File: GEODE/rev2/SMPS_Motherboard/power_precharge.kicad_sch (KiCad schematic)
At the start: 20 parts, among them IC1501 TPS2490DGSRG4, Q1101 SOT233 ZXMP10A13F, Q1102 SOT233 BSS123N

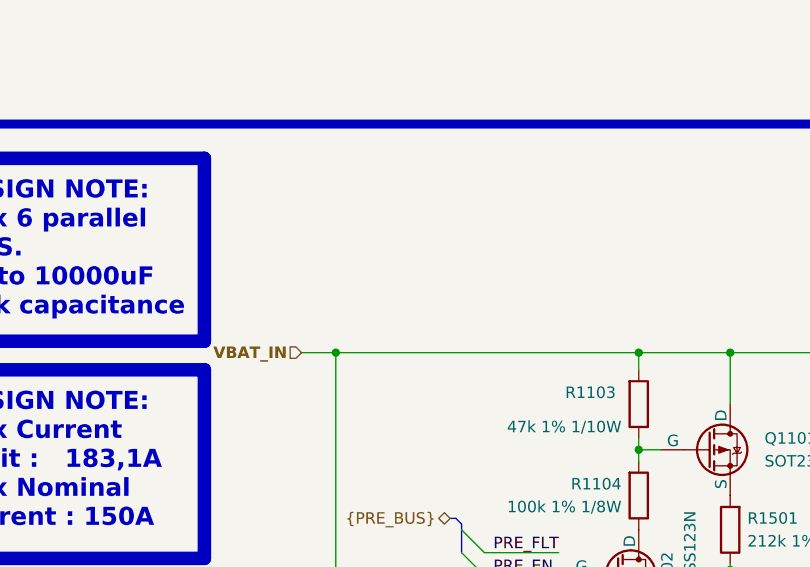
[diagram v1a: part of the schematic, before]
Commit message: changed connectors, removed can, added fuse, disconnected EXTVCC in power generation
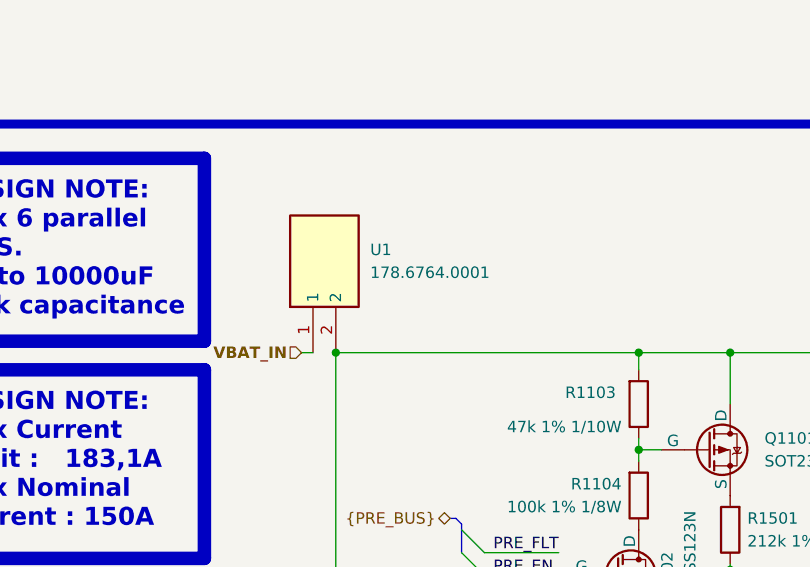
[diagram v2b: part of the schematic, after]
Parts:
- added U1: 178.6764.0001, 17867640001, symbol SamacSys_Parts:178.6764.0001
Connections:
- net VBAT_IN: now also U1.1; no longer C1501.1, NT1101.2, Q1101.3 (D), R1103.2, R1505.1
- new net Vsense_high: C1501.1, NT1101.2, Q1101.3 (D), R1103.2, R1505.1, U1.2
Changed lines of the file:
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@@
+	)
+	(junction
+		(at 87.63 68.58)
+		(diameter 0)
+		(color 0 0 0 0)
 	)
 	(junction
@@
 	)
 	(junction
-		(at 87.63 68.58)
-		(diameter 0)
-		(color 0 0 0 0)
-	)
-	(junction
 		(at 156.21 114.935)
 		(diameter 0)
@@
 	(wire
 		(pts
-			(xy 83.82 68.58) (xy 87.63 68.58)
-		)
-		(stroke
-			(width 0)
-			(type default)
-		)
-	)
-	(wire
-		(pts
 			(xy 87.63 115.57) (xy 87.63 114.935)
 		)
@@
 		(pts
 			(xy 188.595 95.25) (xy 198.755 95.25)
+		)
+		(stroke
+			(width 0)
+			(type default)
+		)
+	)
+	(wire
+		(pts
+			(xy 83.82 68.58) (xy 85.09 68.58)
 		)
 		(stroke
@@
 					(unit 1)
 				)
+			)
+		)
+	)
+	(symbol
+		(lib_id "SamacSys_Parts:178.6764.0001")
+		(at 85.09 68.58 90)
+		(unit 1)
+		(exclude_from_sim no)
+		(in_bom yes)
+		(on_board yes)
+		(dnp no)
+		(fields_autoplaced yes)
+		(property "Reference" "U1"
+			(at 91.44 57.1499 90)
+			(effects
+				(font
+					(size 1.27 1.27)
+				)
+				(justify right)
+			)
+		)
+		(property "Value" "178.6764.0001"
+			(at 91.44 59.6899 90)
+			(effects
+				(font
+					(size 1.27 1.27)
+				)
+				(justify right)
+			)
+		)
+		(property "Footprint" "17867640001"
+			(at 180.01 52.07 0)
+			(effects
+				(font
+					(size 1.27 1.27)
+				)
+				(justify left top)
+				(hide yes)
+			)
+		)
+		(property "Datasheet" "http://www.littelfuse.com/~/media/commercial-vehicle/datasheets/automotive-fuse-holders/mini/littelfuse-fuseholder-mini-fl1-pcb-mount.pdf"
+			(at 280.01 52.07 0)
+			(effects
+				(font
+					(size 1.27 1.27)
+				)
+				(justify left top)
+				(hide yes)
+			)
+		)
+		(property "Description" "LITTELFUSE - 178.6764.0001 - FUSE HOLDER, PCB, FK1 BLADE"
+			(at 85.09 68.58 0)
+			(effects
+				(font
+					(size 1.27 1.27)
+				)
+				(hide yes)
+			)
+		)
+		(property "Height" "15"
+			(at 480.01 52.07 0)
+			(effects
+				(font
+					(size 1.27 1.27)
+				)
+				(justify left top)
+				(hide yes)
+			)
+		)
+		(property "Mouser Part Number" "576-178.6764.0001"
+			(at 580.01 52.07 0)
+			(effects
+				(font
+					(size 1.27 1.27)
+				)
+				(justify left top)
+				(hide yes)
+			)
+		)
+		(property "Mouser Price/Stock" "https://www.mouser.co.uk/ProductDetail/Littelfuse/178.6764.0001?qs=gu7KAQ731UTQ5alyjBY5mw%3D%3D"
+			(at 680.01 52.07 0)
+			(effects
+				(font
+					(size 1.27 1.27)
+				)
+				(justify left top)
+				(hide yes)
+			)
+		)
+		(property "Manufacturer_Name" "LITTELFUSE"
+			(at 780.01 52.07 0)
+			(effects
+				(font
+					(size 1.27 1.27)
+				)
+				(justify left top)
+				(hide yes)
+			)
+		)
+		(property "Manufacturer_Part_Number" "178.6764.0001"
+			(at 880.01 52.07 0)
+			(effects
+				(font
+					(size 1.27 1.27)
+				)
+				(justify left top)
+				(hide yes)
+			)
+		)
+		(pin "1"
+		)
+		(pin "2"
+		)
+		(instances
+			(project ""
+				(path "/0650c7a8-acba-429c-9f8e-eec0baf0bc1c/fede4c36-00cc-4d3d-b71c-5243ba232202/22c274db-2ebb-4584-9395-db6ed9f74837"
+					(reference "U1")
+					(unit 1)
+				)

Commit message: replaced output connectors, added UART connector, removed fuse - schematics
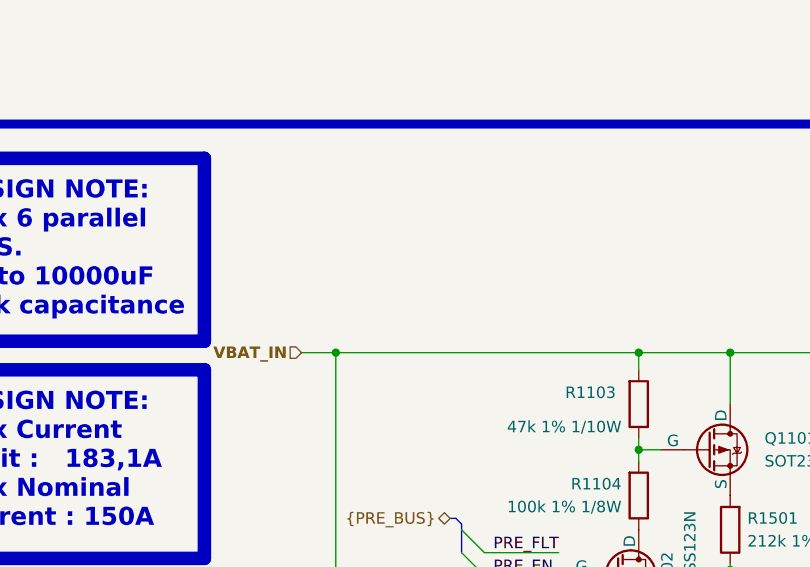
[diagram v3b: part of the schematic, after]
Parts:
- removed U1: 178.6764.0001, 17867640001, symbol SamacSys_Parts:178.6764.0001
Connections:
- net Vsense_high is gone; now on net VBAT_IN: C1501.1, NT1101.2, Q1101.3 (D), R1103.2, R1505.1
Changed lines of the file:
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@@
+	)
+	(junction
+		(at 231.14 68.58)
+		(diameter 0)
+		(color 0 0 0 0)
+	)
+	(junction
+		(at 131.445 92.71)
+		(diameter 0)
+		(color 0 0 0 0)
+	)
+	(junction
+		(at 222.25 114.935)
+		(diameter 0)
+		(color 0 0 0 0)
+	)
+	(junction
+		(at 131.445 114.935)
+		(diameter 0)
+		(color 0 0 0 0)
+	)
+	(junction
+		(at 200.66 68.58)
+		(diameter 0)
+		(color 0 0 0 0)
+	)
+	(junction
+		(at 231.14 101.6)
+		(diameter 0)
+		(color 0 0 0 0)
+	)
+	(junction
+		(at 255.905 68.58)
+		(diameter 0)
+		(color 0 0 0 0)
+	)
+	(junction
+		(at 138.43 104.775)
+		(diameter 0)
+		(color 0 0 0 0)
+	)
+	(junction
+		(at 156.21 114.935)
+		(diameter 0)
+		(color 0 0 0 0)
+	)
+	(junction
+		(at 224.79 68.58)
+		(diameter 0)
+		(color 0 0 0 0)
+	)
+	(junction
+		(at 147.955 114.935)
+		(diameter 0)
+		(color 0 0 0 0)
+	)
+	(junction
+		(at 242.57 68.58)
+		(diameter 0)
+		(color 0 0 0 0)
+	)
+	(junction
+		(at 121.285 79.375)
+		(diameter 0)
+		(color 0 0 0 0)
+	)
+	(junction
+		(at 242.57 114.935)
+		(diameter 0)
+		(color 0 0 0 0)
+	)
+	(junction
+		(at 213.995 97.79)
+		(diameter 0)
+		(color 0 0 0 0)
+	)
+	(junction
+		(at 176.53 68.58)
+		(diameter 0)
+		(color 0 0 0 0)
 	)
 	(junction
@@
 		(color 0 0 0 0)
 	)
-	(junction
-		(at 231.14 68.58)
-		(diameter 0)
-		(color 0 0 0 0)
-	)
-	(junction
-		(at 131.445 92.71)
-		(diameter 0)
-		(color 0 0 0 0)
-	)
-	(junction
-		(at 222.25 114.935)
-		(diameter 0)
-		(color 0 0 0 0)
-	)
-	(junction
-		(at 131.445 114.935)
-		(diameter 0)
-		(color 0 0 0 0)
-	)
-	(junction
-		(at 200.66 68.58)
-		(diameter 0)
-		(color 0 0 0 0)
-	)
-	(junction
-		(at 231.14 101.6)
-		(diameter 0)
-		(color 0 0 0 0)
-	)
-	(junction
-		(at 255.905 68.58)
-		(diameter 0)
-		(color 0 0 0 0)
-	)
-	(junction
-		(at 138.43 104.775)
-		(diameter 0)
-		(color 0 0 0 0)
-	)
-	(junction
-		(at 156.21 114.935)
-		(diameter 0)
-		(color 0 0 0 0)
-	)
-	(junction
-		(at 224.79 68.58)
-		(diameter 0)
-		(color 0 0 0 0)
-	)
-	(junction
-		(at 147.955 114.935)
-		(diameter 0)
-		(color 0 0 0 0)
-	)
-	(junction
-		(at 242.57 68.58)
-		(diameter 0)
-		(color 0 0 0 0)
-	)
-	(junction
-		(at 121.285 79.375)
-		(diameter 0)
-		(color 0 0 0 0)
-	)
-	(junction
-		(at 242.57 114.935)
-		(diameter 0)
-		(color 0 0 0 0)
-	)
-	(junction
-		(at 213.995 97.79)
-		(diameter 0)
-		(color 0 0 0 0)
-	)
-	(junction
-		(at 176.53 68.58)
-		(diameter 0)
-		(color 0 0 0 0)
-	)
 	(bus_entry
 		(at 101.6 88.265)
@@
 	(wire
 		(pts
-			(xy 83.82 68.58) (xy 85.09 68.58)
+			(xy 83.82 68.58) (xy 87.63 68.58)
 		)
 		(stroke
@@
 					(unit 1)
 				)
-			)
-		)
-	)
-	(symbol
-		(lib_id "SamacSys_Parts:178.6764.0001")
-		(at 85.09 68.58 90)
-		(unit 1)
-		(exclude_from_sim no)
-		(in_bom yes)
-		(on_board yes)
-		(dnp no)
-		(fields_autoplaced yes)
-		(property "Reference" "U1"
-			(at 91.44 57.1499 90)
-			(effects
-				(font
-					(size 1.27 1.27)
-				)
-				(justify right)
-			)
-		)
-		(property "Value" "178.6764.0001"
-			(at 91.44 59.6899 90)
-			(effects
-				(font
-					(size 1.27 1.27)
-				)
-				(justify right)
-			)
-		)
-		(property "Footprint" "17867640001"
-			(at 180.01 52.07 0)
-			(effects
-				(font
-					(size 1.27 1.27)
-				)
-				(justify left top)
-				(hide yes)
-			)
-		)
-		(property "Datasheet" "http://www.littelfuse.com/~/media/commercial-vehicle/datasheets/automotive-fuse-holders/mini/littelfuse-fuseholder-mini-fl1-pcb-mount.pdf"
-			(at 280.01 52.07 0)
-			(effects
-				(font
-					(size 1.27 1.27)
-				)
-				(justify left top)
-				(hide yes)
-			)
-		)
-		(property "Description" "LITTELFUSE - 178.6764.0001 - FUSE HOLDER, PCB, FK1 BLADE"
-			(at 85.09 68.58 0)
-			(effects
-				(font
-					(size 1.27 1.27)
-				)
-				(hide yes)
-			)
-		)
-		(property "Height" "15"
-			(at 480.01 52.07 0)
-			(effects
-				(font
-					(size 1.27 1.27)
-				)
-				(justify left top)
-				(hide yes)
-			)
-		)
-		(property "Mouser Part Number" "576-178.6764.0001"
-			(at 580.01 52.07 0)
-			(effects
-				(font
-					(size 1.27 1.27)
-				)
-				(justify left top)
-				(hide yes)
-			)
-		)
-		(property "Mouser Price/Stock" "https://www.mouser.co.uk/ProductDetail/Littelfuse/178.6764.0001?qs=gu7KAQ731UTQ5alyjBY5mw%3D%3D"
-			(at 680.01 52.07 0)
-			(effects
-				(font
-					(size 1.27 1.27)
-				)
-				(justify left top)
-				(hide yes)
-			)
-		)
-		(property "Manufacturer_Name" "LITTELFUSE"
-			(at 780.01 52.07 0)
-			(effects
-				(font
-					(size 1.27 1.27)
-				)
-				(justify left top)
-				(hide yes)
-			)
-		)
-		(property "Manufacturer_Part_Number" "178.6764.0001"
-			(at 880.01 52.07 0)
-			(effects
-				(font
-					(size 1.27 1.27)
-				)
-				(justify left top)
-				(hide yes)
-			)
-		)
-		(pin "1"
-		)
-		(pin "2"
-		)
-		(instances
-			(project ""
-				(path "/0650c7a8-acba-429c-9f8e-eec0baf0bc1c/fede4c36-00cc-4d3d-b71c-5243ba232202/22c274db-2ebb-4584-9395-db6ed9f74837"
-					(reference "U1")
-					(unit 1)
-				)
